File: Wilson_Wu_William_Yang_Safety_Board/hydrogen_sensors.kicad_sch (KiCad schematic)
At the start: 10 parts, among them J10 BH05B-XASK-BN_LF__SN_, J5 Molex Micro-Fit 4 Pin, J9 Molex Micro-Fit 4 Pin, U9 100 ohm

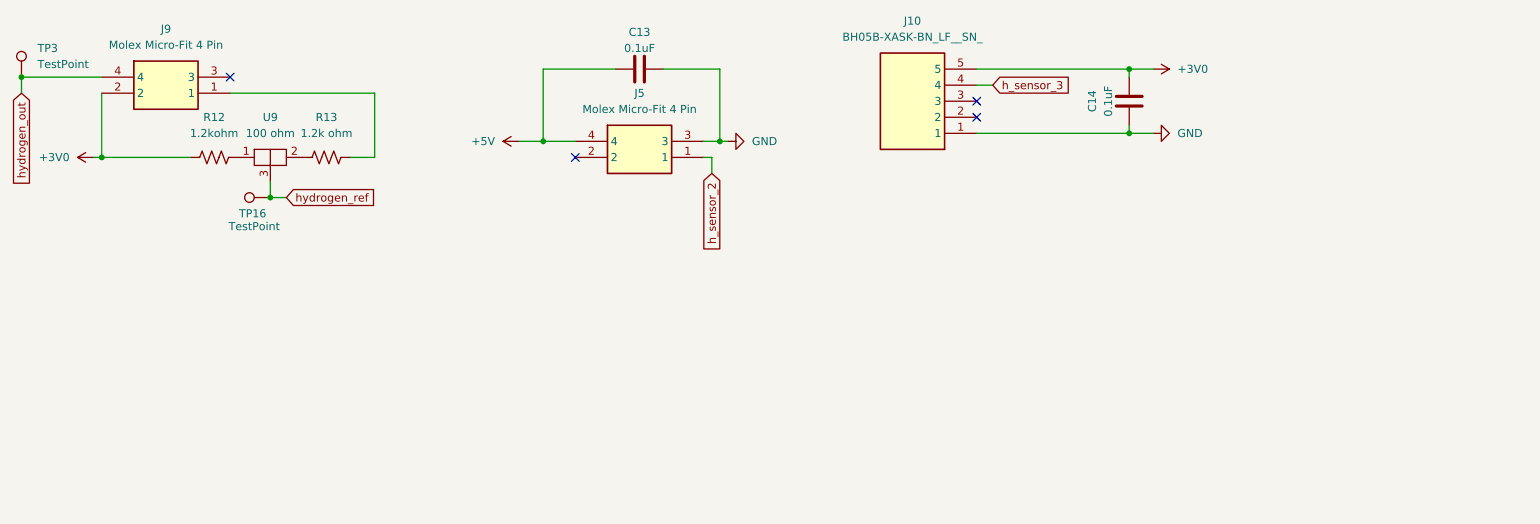
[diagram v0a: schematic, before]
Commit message: hsensor schematic changes
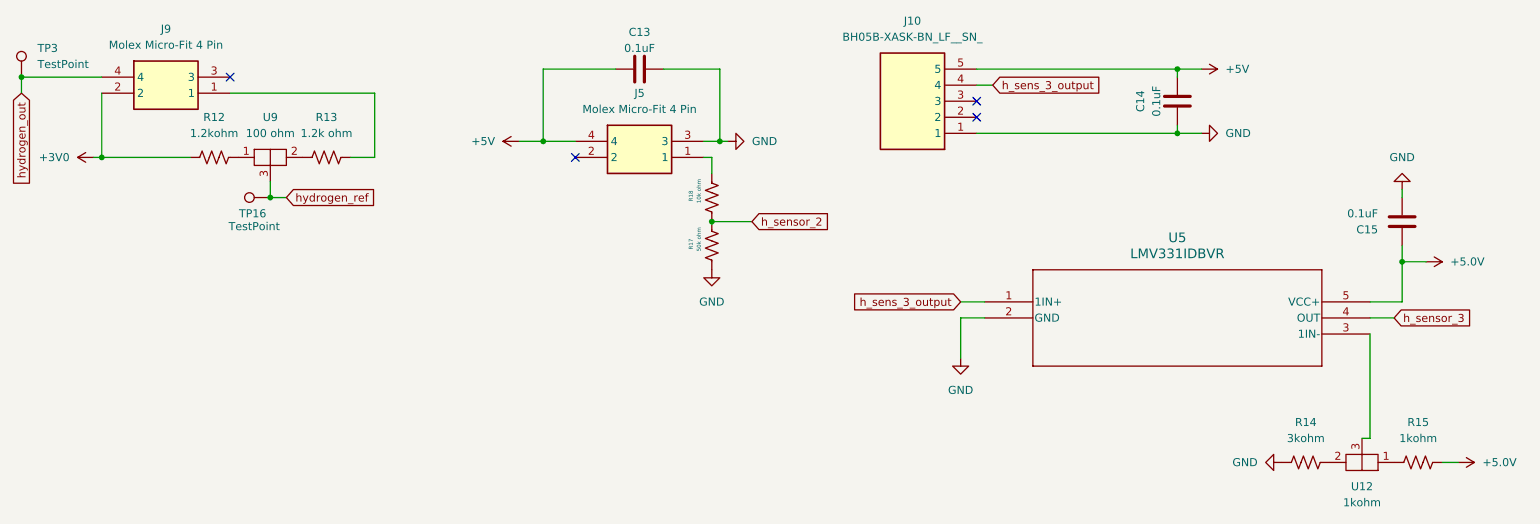
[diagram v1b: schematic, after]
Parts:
- added C15: 0.1uF, Capacitor_SMD:C_0805_2012Metric, symbol Device:C
- added R14: 3kohm, Resistor_SMD:R_0805_2012Metric, symbol Device:R_US
- added R15: 1kohm, Resistor_SMD:R_0805_2012Metric, symbol Device:R_US
- added R17: 50k ohm, Resistor_SMD:R_0805_2012Metric, symbol Device:R_US
- added R18: 10k ohm, Resistor_SMD:R_0805_2012Metric, symbol Device:R_US
- added U12: 1kohm, Potentiometer_THT:Potentiometer_Vishay_T73XW_Horizontal, symbol SMV_Custom:Potentiometer_Custom
- added U5: LMV331IDBVR, lmv33_comparator:DBV5, symbol comparator:LMV331IDBVR
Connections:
- net +3V0: no longer C14.2, J10.5
- net +5V: now also C14.2, J10.5
- net GND: now also C15.1, R14.2, R17.1, U5.2 (GND)
- net h_sensor_2: now also R17.2, R18.1; no longer J5.1
- net h_sensor_3: now also U5.4 (OUT); no longer J10.4
- new net: J5.1, R18.2
- new net: R15.2, U12.1
- new net: R14.1, U12.2
- new net: U12.3, U5.3 (1IN-)
- new net +5.0V: C15.2, R15.1, U5.5 (VCC+)
- new net h_sens_3_output: J10.4, U5.1 (1IN+)
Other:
- moved on the sheet: C14

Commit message: sch to pcb
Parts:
- renumbered R14 to R24, R15 to R25
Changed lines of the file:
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@@
 		(dnp no)
 		(fields_autoplaced yes)
-		(property "Reference" "R15"
+		(property "Reference" "R25"
 			(at 267.97 86.36 90)
 			(effects
@@
 			(project "Wilson_Wu_William_Yang_Safety_Board"
 				(path "/fa857c32-0741-4b91-b122-1a57686bb514/a02d46db-e0b8-42dd-a666-3d9580ac435e"
-					(reference "R15")
+					(reference "R25")
 					(unit 1)
 				)
@@
 		(dnp no)
 		(fields_autoplaced yes)
-		(property "Reference" "R14"
+		(property "Reference" "R24"
 			(at 250.19 86.36 90)
 			(effects
@@
 			(project "Wilson_Wu_William_Yang_Safety_Board"
 				(path "/fa857c32-0741-4b91-b122-1a57686bb514/a02d46db-e0b8-42dd-a666-3d9580ac435e"
-					(reference "R14")
-					(unit 1)
-				)
+					(reference "R24")
+					(unit 1)
+				)

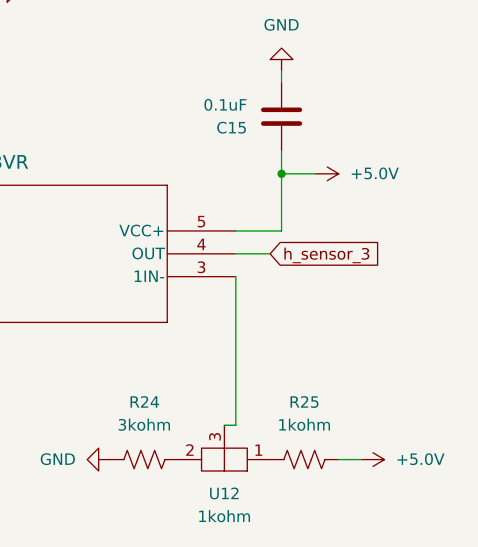
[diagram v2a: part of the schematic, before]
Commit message: Layout connections
mostly done, final connections at the inverter and size might be reducable
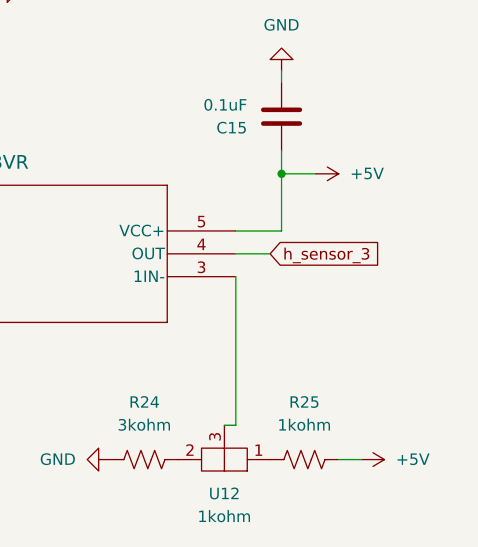
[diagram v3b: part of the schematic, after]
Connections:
- net +5.0V is gone; now on net +5V: C15.2, R25.1, U5.5 (VCC+)
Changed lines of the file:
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@@
 			)
 		)
-		(property "Value" "+5.0V"
+		(property "Value" "+5V"
 			(at 278.13 92.7099 90)
 			(effects
@@
 			)
 		)
-		(property "Value" "+5.0V"
+		(property "Value" "+5V"
 			(at 273.05 60.9601 90)
 			(effects
